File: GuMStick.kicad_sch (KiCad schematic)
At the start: 31 parts, among them Q1 AO3401A, U1 XIAO-nRF52840-SMD, U2 Wio-SX1262, U3 HX PM2.54-1X4P WT, U5 BQ25606RGER

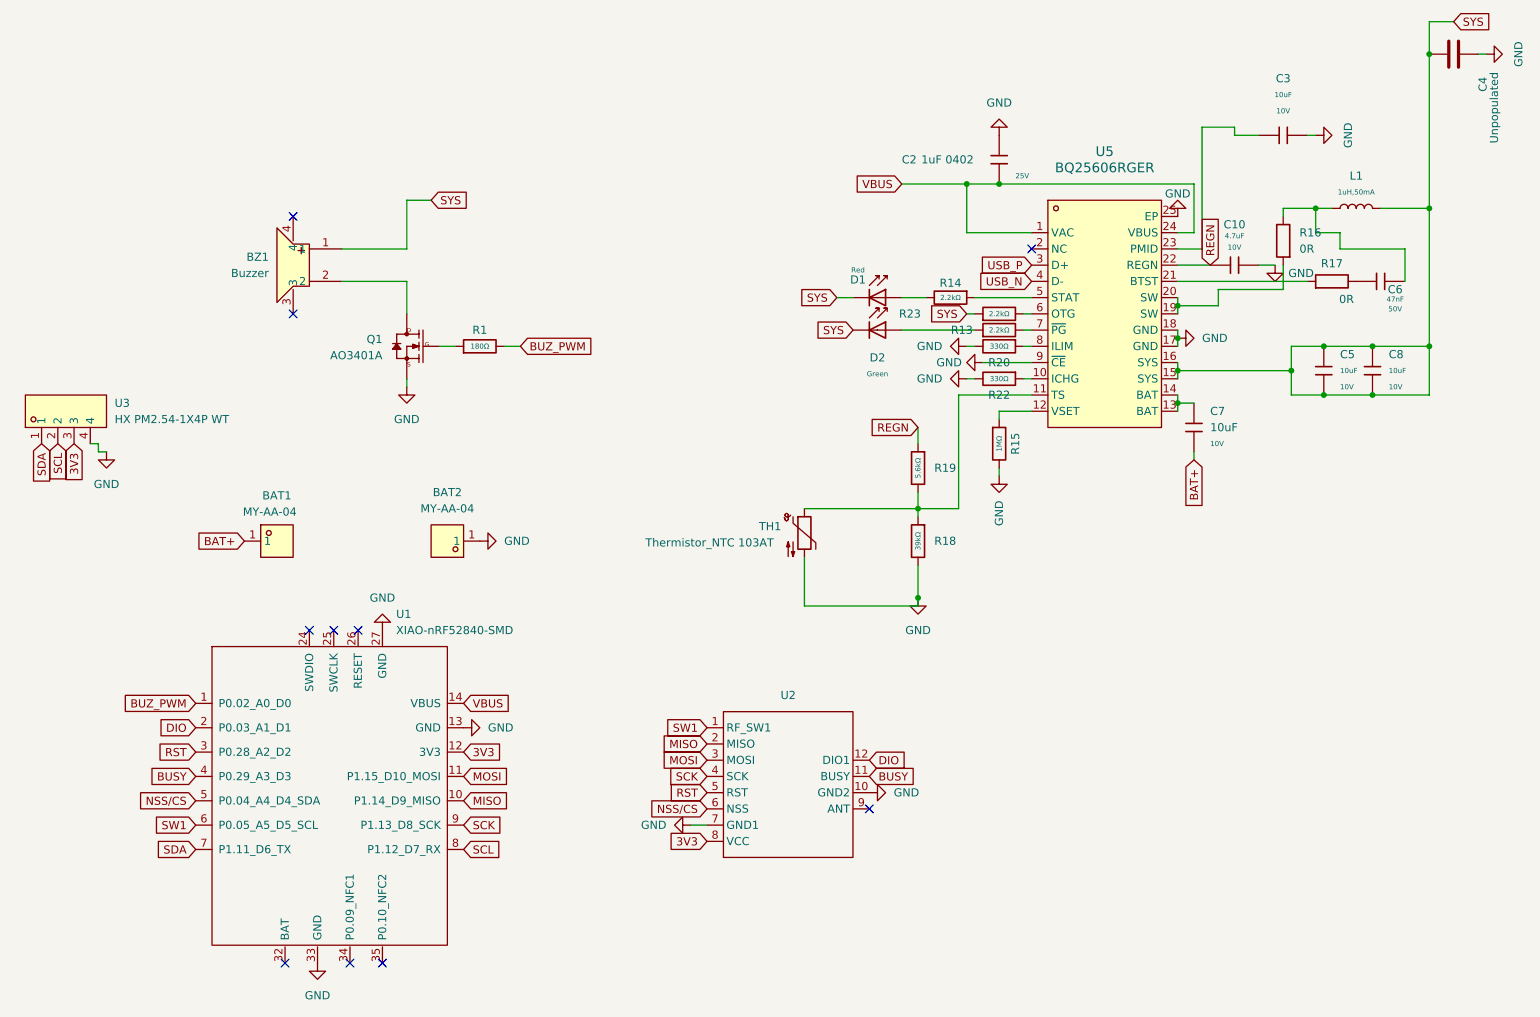
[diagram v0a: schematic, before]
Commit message: Schematic changes, PCB changes not yet complete. Removed error with debounce capacitor in series with Bat+, should have been parallel, prevented system from working. Added a second mosfet for reverse polarity protection (learned to put that in the hard way). Increased RICHG resistor value to lower the charging current to 1A, the battery was getting warm while charging. Future PCB changes will reflect this and move the thermistor pads to the back of the board where they're easier to access for soldering.
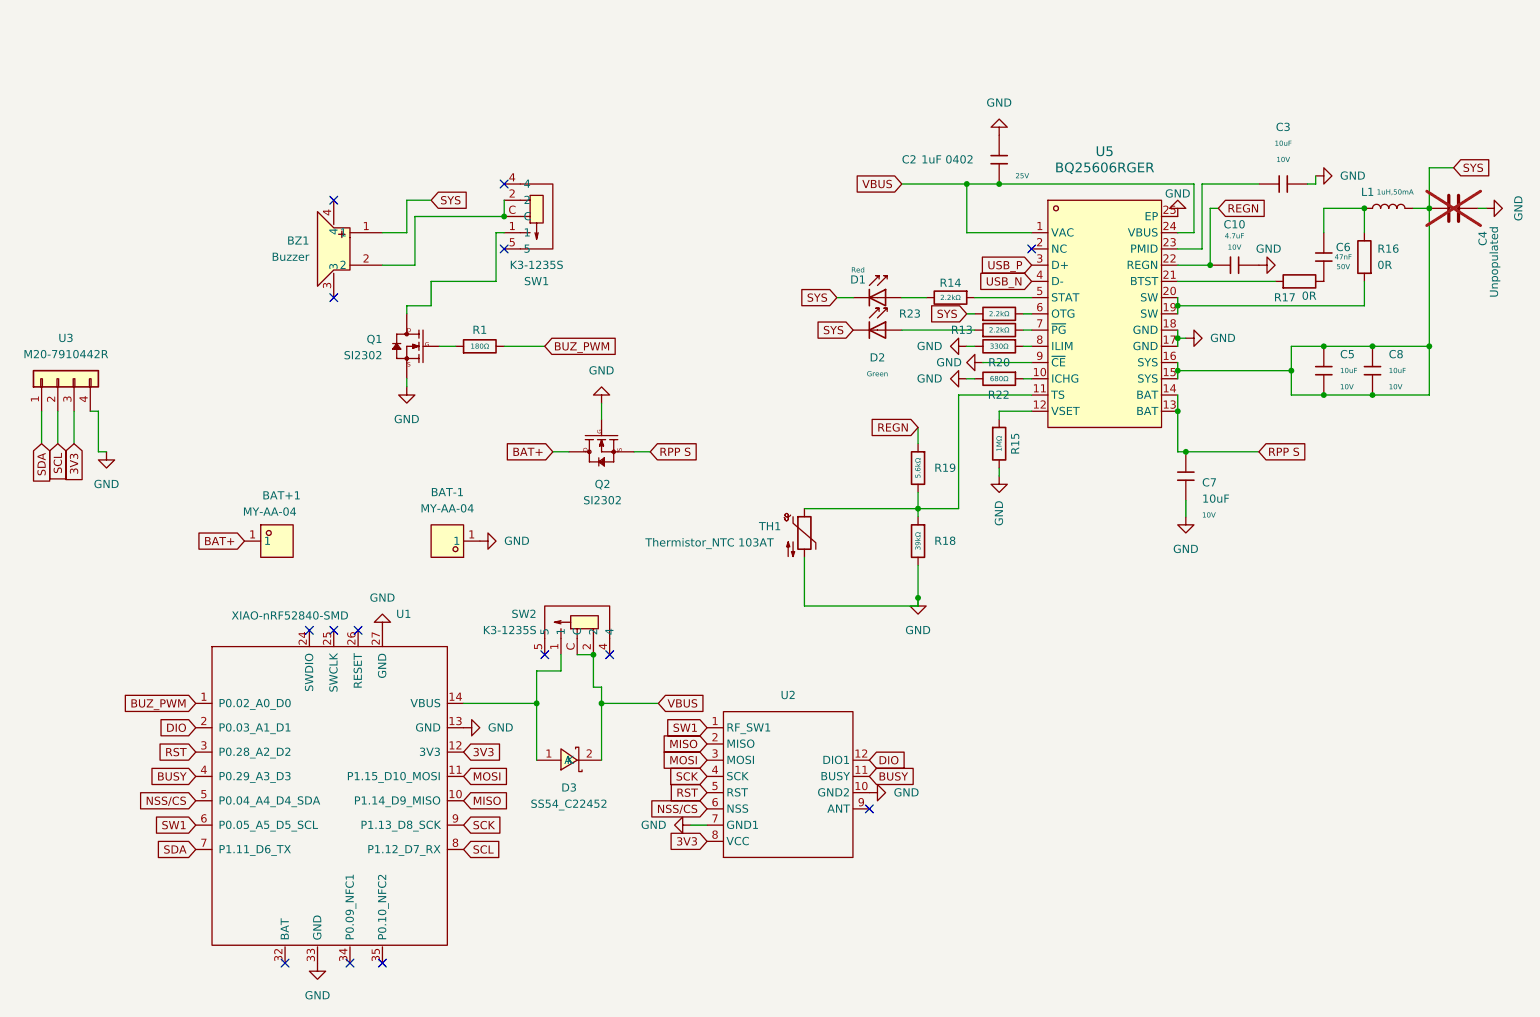
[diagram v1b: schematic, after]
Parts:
- added D3: SS54_C22452, easyeda2kicad:SMA_L4.4-W2.8-LS5.4-R-RD, symbol easyeda2kicad:SS54_C22452
- added Q2: SI2302, Package_TO_SOT_SMD:SOT-23, symbol OPL_Discrete_Semiconductor:SMD-MOSFET-N-CH-20V-2.1A-CJ2302_SOT-23_
- added SW1, SW2: K3-1235S, easyeda2kicad:SW-SMD_MK-11C04-G013, symbol easyeda2kicad:MK-11C04-G013
- BAT+1: renamed from BAT1; footprint easyeda2kicad:BAT-SMD_MY-AAA-06 -> easyeda2kicad:BAT-SMD_MY-AA-04
- BAT-1: renamed from BAT2; footprint easyeda2kicad:BAT-SMD_MY-AAA-06 -> easyeda2kicad:BAT-SMD_MY-AA-04
- BZ1: MANUFACTURER (none) -> CUI Inc.; MAXIMUM_PACKAGE_HEIGHT (none) -> 4.00mm; PARTREV (none) -> 1.0; STANDARD (none) -> Manufacturer Recommendations
- C10: MPN (none) -> CL05A475MP5NRNC
- C2: MPN (none) -> CL05A105KA5NQNC
- C3, C5, C7, C8: MPN (none) -> CL10A106KP8NNNC
- C4: now not fitted
- C6: MPN (none) -> CL10B473KB8NNNC
- D1: footprint PCM_JLCPCB:D_0603 -> PCM_JLCPCB:D_0805; symbol PCM_JLCPCB-Diodes:LED,0603,Red -> PCM_JLCPCB-Diodes:LED,0805,Red; Category Optocouplers & LEDs & Infrared,Light Emitting Diodes (LED) -> Optoelectronics,Light Emitting Diodes (LED); Diode Configuration (none) -> Independent Diode; Dominant Wavelength (none) -> 615nm~630nm; Emitted Color (none) -> Red; Forward Current (none) -> 25mA; Forward Voltage (VF) (none) -> 1.6V~2.6V; LCSC C2286 -> C84256; Lens Color (none) -> Colorless Transparent Lens; Luminous Intensity (none) -> 67mcd~195mcd; MPN (none) -> NCD0805R1; Manufacturer Hubei KENTO Elec -> Foshan NationStar Optoelectronics; Operating Temperature (none) -> -30°C~+85°C; Part KT-0603R -> (none); Power Dissipation (none) -> 65mW; Price 0.009USD -> 0.016USD; Stock 5373336 -> 2976925; Viewing Angle (none) -> 130°
- D2: MPN (none) -> KT-0805G
- L1: MPN (none) -> SDFL2012Q1R0KTF
- Q1: value AO3401A -> SI2302; MPN CJ2302 -> SI2302CDS-T1-GE3; Manufacturer (none) -> Vishay; SKU 305030015 -> (none)
- R1: MPN (none) -> 0603WAF1800T5E
- R13, R14, R23: MPN (none) -> 0402WGF2201TCE
- R15: MPN (none) -> 0402WGF1004TCE
- R16, R17: MPN (none) -> 0603WAF0000T5E
- R18: MPN (none) -> 0603WAF3902T5E
- R19: MPN (none) -> 0603WAF5601T5E
- R20: MPN (none) -> 0402WGF3300TCE
- R22: value 330Ω -> 680Ω; symbol PCM_JLCPCB-Resistors:0402,330Ω -> PCM_JLCPCB-Resistors:0402,680Ω; Class Basic Component -> Preferred Component; LCSC C25104 -> C25130; MPN (none) -> 0402WGF3300TCE; Part 0402WGF3300TCE -> 0402WGF6800TCE; Resistance 330Ω -> 680Ω; Stock 1159127 -> 315941
- TH1: MPN (none) -> 103AT-4-70374; Manufacturer (none) -> Semitec
- U1: MPN (none) -> 102010448; Manufacturer (none) -> Seeed Studio
- U2: MPN (none) -> Wio-SX1262
- U3: value HX PM2.54-1X4P WT -> M20-7910442R; footprint easyeda2kicad:CONN-SMD_4P-P2.54_HX-PM2.54-1X4PWT -> M20_7910442R 4 pin Header:MF254RS-11-04-0743 XFCN 4 Pin Machined Header; symbol easyeda2kicad:HXPM2.54-1X4PWT -> M20-7910442R 4 pin Header:MF254RS-11-04-0743_4_pin_Machined_Header; LCSC Part C46061768 -> (none); MPN HX PM2.54-1x4P WT -> MF254RS-11-04-0743; Manufacturer hanxia(韩下) -> XFCN
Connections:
- net BAT+: now also Q2.3 (D); no longer C7.2
- net GND: now also C7.2, Q2.1 (G)
- net VBUS: now also D3.2 (K), SW2.2, SW2.C; no longer U1.14 (VBUS)
- net RPP S: now reaches C7.1, U5.13 (BAT), U5.14 (BAT)
- net RPP S: now also Q2.2 (S)
- net at Q1.3 (D): now also SW1.1; no longer BZ1.2
- new net: D3.1 (A), SW2.1, U1.14 (VBUS)
- new net: BZ1.2, SW1.2, SW1.C
- no-connect marks 10 -> 14
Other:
- moved on the sheet: BZ1, C3, C6, C7, L1, R16, R17
